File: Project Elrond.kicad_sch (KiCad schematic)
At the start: 15 parts, among them U104 UA741, U106 UA741

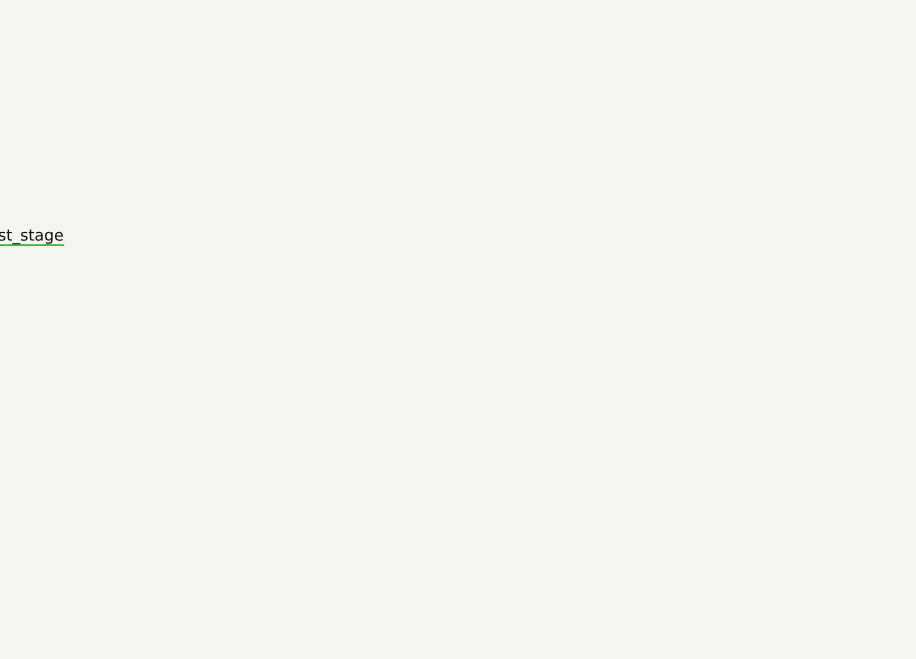
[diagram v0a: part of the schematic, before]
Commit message: Add INA163UA preamp stage
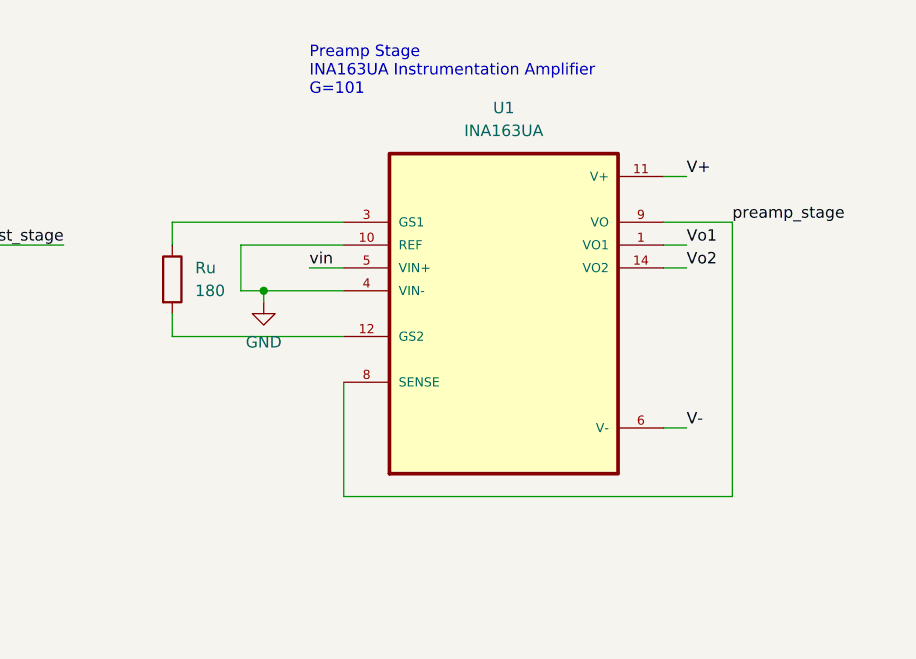
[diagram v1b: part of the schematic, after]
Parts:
- added Ru: 180, symbol Device:R
- added U1: INA163UA, SOIC127P600X175-14N, symbol INA163UA:INA163UA
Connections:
- net GND: now also U1.10 (REF), U1.4 (VIN-)
- net V+: now also U1.11 (V+)
- net V-: now also U1.6 (V-)
- net vin: now also U1.5 (VIN+)
- new net: Ru.1, U1.3 (GS1)
- new net: Ru.2, U1.12 (GS2)
- new net Vo1: U1.1 (VO1)
- new net Vo2: U1.14 (VO2)
- new net preamp_stage: U1.8 (SENSE), U1.9 (VO)
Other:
- note added: "Preamp Stage INA163UA Instrumentation Amplifier G=101"
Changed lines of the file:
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@@
   (junction (at 222.885 125.095) (diameter 0) (color 0 0 0 0)
   )
+  (junction (at 166.37 50.8) (diameter 0) (color 0 0 0 0)
+  )
   (junction (at 181.61 137.795) (diameter 0) (color 0 0 0 0)
   )
@@
     (stroke (width 0) (type default) (color 0 0 0 0))
   )
+  (wire (pts (xy 166.37 50.8) (xy 175.26 50.8))
+    (stroke (width 0) (type default) (color 0 0 0 0))
+  )
+  (wire (pts (xy 213.36 38.1) (xy 210.82 38.1))
+    (stroke (width 0) (type default) (color 0 0 0 0))
+  )
+  (wire (pts (xy 218.44 73.66) (xy 218.44 43.18))
+    (stroke (width 0) (type default) (color 0 0 0 0))
+  )
   (wire (pts (xy 198.12 104.14) (xy 198.12 122.555))
     (stroke (width 0) (type default) (color 0 0 0 0))
   )
+  (wire (pts (xy 175.26 60.96) (xy 175.26 73.66))
+    (stroke (width 0) (type default) (color 0 0 0 0))
+  )
+  (wire (pts (xy 213.36 48.26) (xy 210.82 48.26))
+    (stroke (width 0) (type default) (color 0 0 0 0))
+  )
   (wire (pts (xy 100.33 45.72) (xy 109.22 45.72))
     (stroke (width 0) (type default) (color 0 0 0 0))
@@
     (stroke (width 0) (type default) (color 0 0 0 0))
   )
+  (wire (pts (xy 166.37 50.8) (xy 166.37 52.07))
+    (stroke (width 0) (type default) (color 0 0 0 0))
+  )
+  (wire (pts (xy 163.83 45.72) (xy 175.26 45.72))
+    (stroke (width 0) (type default) (color 0 0 0 0))
+  )
   (wire (pts (xy 97.79 120.015) (xy 97.79 125.73))
     (stroke (width 0) (type default) (color 0 0 0 0))
@@
     (stroke (width 0) (type default) (color 0 0 0 0))
   )
+  (wire (pts (xy 175.26 43.18) (xy 156.21 43.18))
+    (stroke (width 0) (type default) (color 0 0 0 0))
+  )
   (wire (pts (xy 97.79 120.015) (xy 102.87 120.015))
     (stroke (width 0) (type default) (color 0 0 0 0))
@@
     (stroke (width 0) (type default) (color 0 0 0 0))
   )
+  (wire (pts (xy 163.83 50.8) (xy 166.37 50.8))
+    (stroke (width 0) (type default) (color 0 0 0 0))
+  )
   (wire (pts (xy 97.79 135.255) (xy 97.79 136.525))
     (stroke (width 0) (type default) (color 0 0 0 0))
   )
+  (wire (pts (xy 163.83 45.72) (xy 163.83 50.8))
+    (stroke (width 0) (type default) (color 0 0 0 0))
+  )
   (wire (pts (xy 181.61 122.555) (xy 186.69 122.555))
     (stroke (width 0) (type default) (color 0 0 0 0))
@@
     (stroke (width 0) (type default) (color 0 0 0 0))
   )
+  (wire (pts (xy 156.21 55.88) (xy 175.26 55.88))
+    (stroke (width 0) (type default) (color 0 0 0 0))
+  )
   (wire (pts (xy 97.79 97.155) (xy 97.79 120.015))
     (stroke (width 0) (type default) (color 0 0 0 0))
@@
     (stroke (width 0) (type default) (color 0 0 0 0))
   )
+  (wire (pts (xy 213.36 45.72) (xy 210.82 45.72))
+    (stroke (width 0) (type default) (color 0 0 0 0))
+  )
+  (wire (pts (xy 175.26 73.66) (xy 218.44 73.66))
+    (stroke (width 0) (type default) (color 0 0 0 0))
+  )
   (wire (pts (xy 49.53 38.1) (xy 49.53 41.275))
     (stroke (width 0) (type default) (color 0 0 0 0))
@@
     (stroke (width 0) (type default) (color 0 0 0 0))
   )
+  (wire (pts (xy 171.45 48.26) (xy 175.26 48.26))
+    (stroke (width 0) (type default) (color 0 0 0 0))
+  )
+  (wire (pts (xy 213.36 66.04) (xy 210.82 66.04))
+    (stroke (width 0) (type default) (color 0 0 0 0))
+  )
   (wire (pts (xy 196.215 99.695) (xy 181.61 99.695))
     (stroke (width 0) (type default) (color 0 0 0 0))
@@
     (stroke (width 0) (type default) (color 0 0 0 0))
   )
+  (wire (pts (xy 156.21 53.34) (xy 156.21 55.88))
+    (stroke (width 0) (type default) (color 0 0 0 0))
+  )
   (wire (pts (xy 222.885 104.14) (xy 222.885 125.095))
     (stroke (width 0) (type default) (color 0 0 0 0))
@@
     (stroke (width 0) (type default) (color 0 0 0 0))
   )
+  (wire (pts (xy 156.21 43.18) (xy 156.21 45.72))
+    (stroke (width 0) (type default) (color 0 0 0 0))
+  )
   (wire (pts (xy 203.835 104.14) (xy 198.12 104.14))
     (stroke (width 0) (type default) (color 0 0 0 0))
+  )
+  (wire (pts (xy 210.82 43.18) (xy 218.44 43.18))
+    (stroke (width 0) (type default) (color 0 0 0 0))
+  )
+  (text "Preamp Stage\nINA163UA Instrumentation Amplifier\nG=101"
+    (at 171.45 29.21 0)
+    (effects (font (size 1.27 1.27)) (justify left bottom))
   )
   (text "2nd Stage\n2nd order Butterworth\nMultiple-Feedback\n10Hz LPF\nG=10"
@@
     (effects (font (size 1.27 1.27)) (justify right bottom))
   )
+  (label "V-" (at 213.36 66.04 0)
+    (effects (font (size 1.27 1.27)) (justify left bottom))
+  )
+  (label "Vo2" (at 213.36 48.26 0)
+    (effects (font (size 1.27 1.27)) (justify left bottom))
+  )
+  (label "preamp_stage" (at 218.44 43.18 0)
+    (effects (font (size 1.27 1.27)) (justify left bottom))
+  )
   (label "V-" (at 207.645 114.3 270)
     (effects (font (size 1.27 1.27)) (justify right bottom))
@@
     (effects (font (size 1.27 1.27)) (justify left bottom))
   )
+  (label "V+" (at 213.36 38.1 0)
+    (effects (font (size 1.27 1.27)) (justify left bottom))
+  )
   (label "1st_stage" (at 144.145 45.72 180)
     (effects (font (size 1.27 1.27)) (justify right bottom))
@@
   (label "3rd_stage_ua" (at 236.855 125.095 180)
     (effects (font (size 1.27 1.27)) (justify right bottom))
+  )
+  (label "vin" (at 171.45 48.26 0)
+    (effects (font (size 1.27 1.27)) (justify left bottom))
+  )
+  (label "Vo1" (at 213.36 45.72 0)
+    (effects (font (size 1.27 1.27)) (justify left bottom))
   )
   (label "V+" (at 207.645 135.89 90)
@@
     (pin "1")
   )
+  (symbol (lib_id "Device:R") (at 156.21 49.53 0) (unit 1)
+    (in_bom yes) (on_board yes) (fields_autoplaced)
+    (property "Reference" "Ru" (id 0) (at 158.75 48.2599 0)
+      (effects (font (size 1.27 1.27)) (justify left))
+    )
+    (property "Value" "180" (id 1) (at 158.75 50.7999 0)
+      (effects (font (size 1.27 1.27)) (justify left))
+    )
+    (property "Footprint" "" (id 2) (at 154.432 49.53 90)
+      (effects (font (size 1.27 1.27)) hide)
+    )
+    (property "Datasheet" "~" (id 3) (at 156.21 49.53 0)
+      (effects (font (size 1.27 1.27)) hide)
+    )
+    (pin "1")
+    (pin "2")
+  )
   (symbol (lib_id "Device:R") (at 190.5 122.555 270) (unit 1)
     (in_bom yes) (on_board yes) (fields_autoplaced)
@@
     (pin "1")
   )
+  (symbol (lib_id "power:GND") (at 166.37 52.07 0) (unit 1)
+    (in_bom yes) (on_board yes) (fields_autoplaced)
+    (property "Reference" "#PWR?" (id 0) (at 166.37 58.42 0)
+      (effects (font (size 1.27 1.27)) hide)
+    )
+    (property "Value" "GND" (id 1) (at 166.37 56.515 0))
+    (property "Footprint" "" (id 2) (at 166.37 52.07 0)
+      (effects (font (size 1.27 1.27)) hide)
+    )
+    (property "Datasheet" "" (id 3) (at 166.37 52.07 0)
+      (effects (font (size 1.27 1.27)) hide)
+    )
+    (pin "1")
+  )
   (symbol (lib_id "Device:R") (at 200.025 99.695 90) (unit 1)
     (in_bom yes) (on_board yes) (fields_autoplaced)
@@
     (pin "1")
     (pin "2")
+  )
+  (symbol (lib_id "INA163UA:INA163UA") (at 193.04 53.34 0) (unit 1)
+    (in_bom yes) (on_board yes) (fields_autoplaced)
+    (property "Reference" "U1" (id 0) (at 193.04 30.48 0))
+    (property "Value" "INA163UA" (id 1) (at 193.04 33.02 0))
+    (property "Footprint" "SOIC127P600X175-14N" (id 2) (at 193.04 53.34 0)
+      (effects (font (size 1.27 1.27)) (justify left bottom) hide)
+    )
+    (property "Datasheet" "" (id 3) (at 193.04 53.34 0)
+      (effects (font (size 1.27 1.27)) (justify left bottom) hide)
+    )
+    (property "Spice_Primitive" "X" (id 4) (at 193.04 53.34 0)
+      (effects (font (size 1.27 1.27)) hide)
+    )
+    (property "Spice_Model" "INA163" (id 5) (at 193.04 53.34 0)
+      (effects (font (size 1.27 1.27)) hide)
+    )
+    (property "Spice_Netlist_Enabled" "Y" (id 6) (at 193.04 53.34 0)
+      (effects (font (size 1.27 1.27)) hide)
+    )
+    (property "Spice_Lib_File" "INA163.LIB" (id 7) (at 193.04 53.34 0)
+      (effects (font (size 1.27 1.27)) hide)
+    )
+    (pin "1")
+    (pin "10")
+    (pin "11")
+    (pin "12")
+    (pin "14")
+    (pin "3")
+    (pin "4")
+    (pin "5")
+    (pin "6")
+    (pin "8")
+    (pin "9")
   )
   (symbol (lib_id "Device:C") (at 123.825 101.6 90) (unit 1)
@@
       (reference "#PWR0202") (unit 1) (value "~") (footprint "")
     )
+    (path "/c9122bc2-4924-4adc-bd47-bf79eaffc278"
+      (reference "#PWR?") (unit 1) (value "GND") (footprint "")
+    )
     (path "/5b7bf172-b38b-43c4-9fab-75ddd133d087"
       (reference "C106") (unit 1) (value "100n") (footprint "")
@@
       (reference "R205") (unit 1) (value "9.09k") (footprint "")
     )
+    (path "/ac4d1d16-39b5-49ca-bf60-f073f3729ea1"
+      (reference "Ru") (unit 1) (value "180") (footprint "")
+    )
+    (path "/e85fe4eb-16e0-4755-8c8c-cd70900824b1"
+      (reference "U1") (unit 1) (value "INA163UA") (footprint "SOIC127P600X175-14N")
+    )
     (path "/23f791bf-8f6b-48db-8c6a-46c4b7db16f7"
